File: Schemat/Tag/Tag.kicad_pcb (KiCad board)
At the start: 4 copper layers, 60 x 90 mm, 91 parts, among them J1 Conn_Coaxial, J2 USB_C_Receptacle_USB2.0_16P, J3 Conn_01x02_Pin, J4 Conn_01x02_Pin, J5 Conn_01x04_Pin, J6 Conn_01x02_Pin, J7 Conn_01x02_Pin, Q1 AO3401A, Q2 IRLML6344TRPBF, Q3 IRLML6344TRPBF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

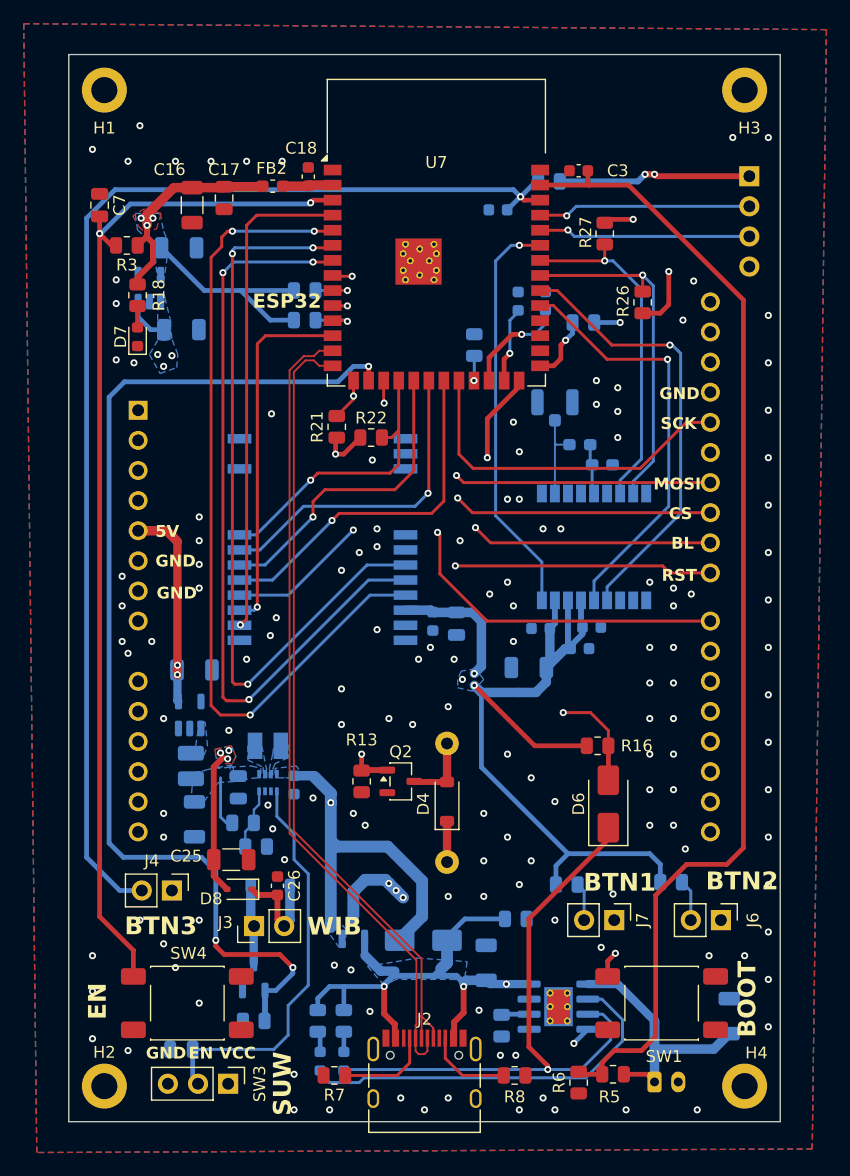
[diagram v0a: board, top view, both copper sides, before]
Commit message: Poprawki 09.05
Zmiana poprowadzenia ścieżek sygnałowych w celu poprawy wylewki GND
Dodatkowe przelotki przy GND układy TPS631000
Dodanie zworek 0R z miedzią na wierzchu dla większości linii sygnałowych (nie dodano dla ścieżek do przycisków, bo tam są pady)
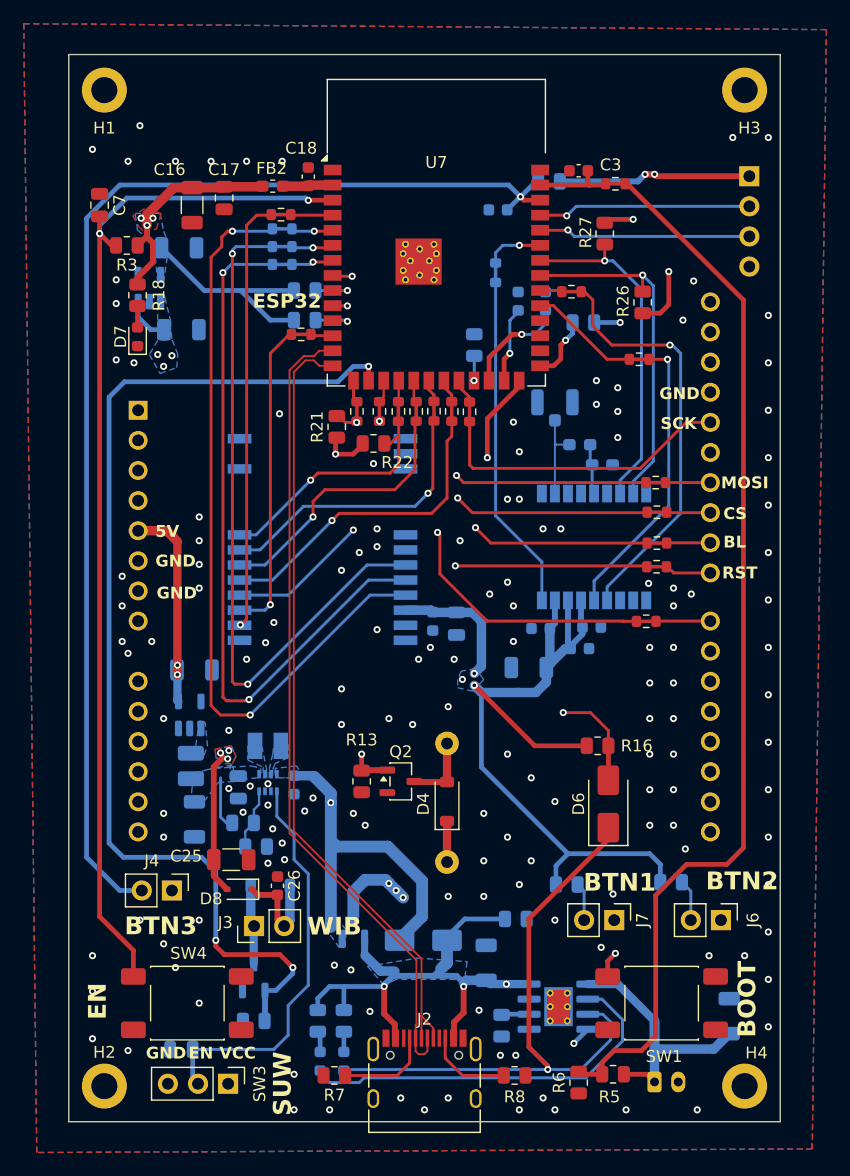
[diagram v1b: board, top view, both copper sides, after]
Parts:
- added JP1: SolderJumper_2_Bridged, Biblioteka:Zworka, F.Cu at (77.8, 80.1)
- added JP10: SolderJumper_2_Bridged, Biblioteka:Zworka, F.Cu at (98.7, 97.8)
- added JP11: SolderJumper_2_Bridged, Biblioteka:Zworka, F.Cu at (99.6, 93.2)
- added JP13: SolderJumper_2_Bridged, Biblioteka:Zworka, B.Cu at (86.0, 68.4)
- added JP14: SolderJumper_2_Bridged, Biblioteka:Zworka, F.Cu at (98.1, 75.7)
- added JP15: SolderJumper_2_Bridged, Biblioteka:Zworka, F.Cu at (92.4, 70.0)
- added JP16: SolderJumper_2_Bridged, Biblioteka:Zworka, F.Cu at (67.9, 63.5)
- added JP17: SolderJumper_2_Bridged, Biblioteka:Zworka, B.Cu at (68.0, 64.7)
- added JP18: SolderJumper_2_Bridged, Biblioteka:Zworka, B.Cu at (68.0, 66.2)
- added JP19: SolderJumper_2_Bridged, Biblioteka:Zworka, B.Cu at (68.0, 67.7)
- added JP2: SolderJumper_2_Bridged, Biblioteka:Zworka, F.Cu at (79.3, 80.1)
- added JP20: SolderJumper_2_Bridged, Biblioteka:Zworka, F.Cu at (69.6, 73.6)
- added JP21: SolderJumper_2_Bridged, Biblioteka:Zworka, F.Cu at (96.1, 60.9)
- added JP22: SolderJumper_2_Bridged, Biblioteka:Zworka, F.Cu at (74.3, 80.1)
- added JP3: SolderJumper_2_Bridged, Biblioteka:Zworka, F.Cu at (80.8, 80.1)
- added JP4: SolderJumper_2_Bridged, Biblioteka:Zworka, F.Cu at (82.3, 80.1)
- added JP5: SolderJumper_2_Bridged, Biblioteka:Zworka, F.Cu at (83.8, 80.1)
- added JP6: SolderJumper_2_Bridged, Biblioteka:Zworka, F.Cu at (99.6, 91.2)
- added JP7: SolderJumper_2_Bridged, Biblioteka:Zworka, F.Cu at (76.2, 80.1)
- added JP8: SolderJumper_2_Bridged, Biblioteka:Zworka, F.Cu at (99.5, 86.1)
- added JP9: SolderJumper_2_Bridged, Biblioteka:Zworka, F.Cu at (99.6, 88.6)
- moved R22 0.54 mm to (75.7, 82.8)
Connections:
- C3 pad 1: V_BAT_meas -> Net-(JP21-B)
- R23 pad 1: W_CS -> Net-(JP9-B)
- R24 pad 2: W_RST -> Net-(JP11-A)
- R25 pad 1: W_BL -> Net-(JP6-A)
- U7 pad 10: W_DC -> Net-(JP10-A)
- U7 pad 11: W_RST -> Net-(JP11-A)
- U7 pad 12: BUSY -> Net-(JP20-B)
- U7 pad 15: NRESET -> Net-(JP22-B)
- U7 pad 17: CHRG -> Net-(JP7-B)
- U7 pad 18: NSS -> Net-(JP1-B)
- U7 pad 19: MOSI -> Net-(JP2-B)
- U7 pad 20: SCK -> Net-(JP3-B)
- U7 pad 21: MISO -> Net-(JP4-B)
- U7 pad 22: W_SCK -> Net-(JP5-B)
- U7 pad 23: W_BL -> Net-(JP6-A)
- U7 pad 31: EXT_INT -> Net-(JP14-A)
- U7 pad 32: TIMEPULSE -> Net-(JP15-A)
- U7 pad 35: RESET_N_GPS -> Net-(JP13-A)
- U7 pad 39: V_BAT_meas -> Net-(JP21-B)
- U7 pad 4: DIO1 -> Net-(JP16-B)
- U7 pad 5: DIO2 -> Net-(JP17-B)
- U7 pad 6: RXEN -> Net-(JP18-B)
- U7 pad 7: TXEN -> Net-(JP19-B)
- U7 pad 8: W_MOSI -> Net-(JP8-B)
- U7 pad 9: W_CS -> Net-(JP9-B)
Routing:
- net W_DC: track 51.6 -> 4.49 mm, vias 2 -> 0
- net W_RST: track 50.4 -> 3.82 mm, vias 2 -> 0
- net Net-(JP10-A): track 0.00 -> 45.2 mm, vias 0 -> 2
- net Net-(JP11-A): track 0.00 -> 44.7 mm, vias 0 -> 2
- net W_CS: track 47.1 -> 3.60 mm, vias 2 -> 0
- net Net-(JP9-B): track 0.00 -> 41.7 mm, vias 0 -> 2
- net W_MOSI: track 43.8 -> 3.68 mm, vias 2 -> 0
- net Net-(JP8-B): track 0.00 -> 38.2 mm, vias 0 -> 2
- net W_BL: track 34.9 -> 3.59 mm, vias 2 -> 0
- net Net-(JP6-A): track 0.00 -> 29.5 mm, vias 0 -> 2
- net EXT_INT: track 35.6 -> 24.5 mm
- net Net-(JP14-A): track 0.00 -> 9.30 mm
- net V_BAT_meas: track 98.1 -> 89.4 mm
- net Net-(JP21-B): track 0.00 -> 6.66 mm
- net RESET_N_GPS: track 34.5 -> 28.3 mm, vias 1 -> 0
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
